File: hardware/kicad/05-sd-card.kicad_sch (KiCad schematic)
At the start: 1 part, among them U6 SD_Card_SPI

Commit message: fix(schematic): sync GPIO labels with config.py (SD_MOSI/MISO, BTN_L/R)
Schematic sheets had stale GPIO annotations:
- SD_MOSI: GPIO36 → GPIO44
- SD_MISO: GPIO37 → GPIO43
- BTN_L: GPIO35 → GPIO45
- BTN_R: GPIO43 → GPIO3

Also update /doc skill to regenerate schematics before auditing.

Co-Authored-By: Claude Opus 4.6 (1M context) <noreply@anthropic.com>
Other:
- note added: "GPIO43"
- note added: "GPIO44"
- note removed: "GPIO36"
- note removed: "GPIO37"
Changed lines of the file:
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@@
   (wire (pts (xy 158.16 106.19) (xy 183.16 106.19)) (stroke (width 0) (type default)))
   (global_label "SD_MOSI" (shape bidirectional) (at 183.16 106.19 0) (effects (font (size 1.27 1.27))) (property "Intersheetrefs" "" (at 0 0 0) (effects (font (size 1.27 1.27)) hide)))
-  (text "GPIO36" (at 198.16 106.19 0) (effects (font (size 1.5 1.5)) (justify left)))
+  (text "GPIO44" (at 198.16 106.19 0) (effects (font (size 1.5 1.5)) (justify left)))
   (wire (pts (xy 158.16 110) (xy 183.16 110)) (stroke (width 0) (type default)))
   (global_label "SD_MISO" (shape bidirectional) (at 183.16 110 0) (effects (font (size 1.27 1.27))) (property "Intersheetrefs" "" (at 0 0 0) (effects (font (size 1.27 1.27)) hide)))
-  (text "GPIO37" (at 198.16 110 0) (effects (font (size 1.5 1.5)) (justify left)))
+  (text "GPIO43" (at 198.16 110 0) (effects (font (size 1.5 1.5)) (justify left)))
   (wire (pts (xy 158.16 113.81) (xy 183.16 113.81)) (stroke (width 0) (type default)))
   (global_label "SD_CLK" (shape bidirectional) (at 183.16 113.81 0) (effects (font (size 1.27 1.27))) (property "Intersheetrefs" "" (at 0 0 0) (effects (font (size 1.27 1.27)) hide)))

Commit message: fix(hw): R4 audit — schematic↔PCB sync guard + 4 fixes + R4-CRIT-1 false-positive closure
Round 4 of the hardware audit found four real schematic/PCB drift bugs
that rounds 1-3 missed because no check cross-validated the two Python
generators. A fifth finding (R4-CRIT-1, "FPC pinout mismatch") turned
out to be a FALSE POSITIVE caused by the landscape FPC pin reversal
(connector_pad = 41 − panel_pin) — verified programmatically against
all 40 J4 pads of the panel datasheet in components.md.

Fixes applied:
  R4-HIGH-1  USBLC6 (U4) + R22/R23 instantiated in power_supply.py —
             previously only in routing.py, invisible to schematic
             review.
  R4-HIGH-2  Display module symbol ref renamed U4 → DS1 in display.py.
             U4 is now cleanly owned by the physical USBLC6 TVS.
  R4-HIGH-3  PAM8403 R20/R21 input bias moved from GND to VREF
             (pin 8) per the datasheet single-ended app circuit.
  R4-CRIT-1  CLOSED as false positive. Both display.py (panel-side)
             and datasheet_specs.py (connector-side) were correct all
             along. Added 41-N reversal documentation at the top of
             both files so the mistake can't be re-raised.
  ERC CRIT   Pre-existing "Power output ↔ Power output" on +5V was
             PWR_FLAG duplicating IP5306 VOUT (already power_out in the
             library symbol). Removed the PWR_FLAG. ERC now 0 critical.

Incidental cleanups required by the new sync guard:
  - mcu.py R3 (external EN pull-up) removed from schematic — already
    DNP in BOM because the WROOM-1 module has an internal pull-up.
  - controls.py D1 BAT54C (MENU combo diode) instantiated in schematic
    to match the PCB routing. MENU button wiring simplified to the
    MENU_K node; there is no dedicated BTN_MENU GPIO (firmware detects
    START+SELECT combo).
  - power_supply.py USB_CC1 / USB_CC2 global labels added so the
    connector-net coverage check sees the full USB-C net set.
  - display.py docstring expanded with the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
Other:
- note added: "v2 TODO: add local 100nF bypass near U6 VCC (R4-MED-1)"
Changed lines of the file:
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@@
   (wire (pts (xy 118 113.81) (xy 137.84 113.81)) (stroke (width 0) (type default)))
   (text "GPIO39" (at 90 115 0) (effects (font (size 1.5 1.5)) (justify left)))
+  (text "v2 TODO: add local 100nF bypass near U6 VCC (R4-MED-1)" (at 90 120 0) (effects (font (size 1.5 1.5)) (justify left)))
   (text "Design Notes:" (at 30 160 0) (effects (font (size 2.54 2.54) bold) (justify left)))
   (text "- SPI bus @ up to 40MHz (ESP32-S3 max for SD)" (at 30 168 0) (effects (font (size 2.54 2.54)) (justify left)))

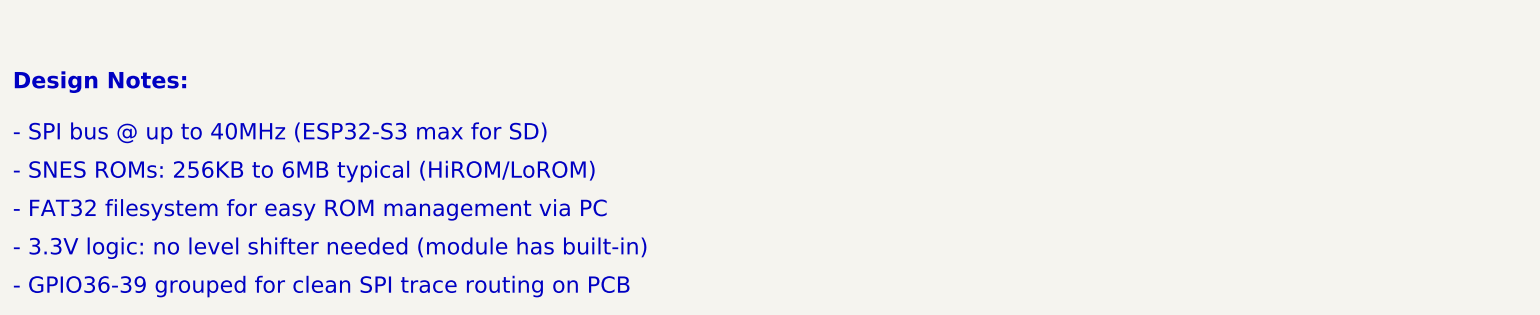
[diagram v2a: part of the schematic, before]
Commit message: docs(R10): close 8 LOW-severity doc-drift findings from Layer 2 audit
Round 10 hardware-audit Layer 2 prose pass found no functional bugs
(0 CRIT/HIGH/MED) but surfaced 8 stale comments and doc-drift items
across schematic generator text labels, datasheet_specs.py function
strings, verify_strapping_pins.py RC timing math, and
snes-optimization.md. All fixed in this single commit — no PCB
regeneration, no routing/geometry changes.

- R10-LOW-1: mcu.py GPIO table labeled "GPIO26-32 = Octal PSRAM" but
  those are actually Octal Flash pins on ESP32-S3-WROOM-1 N16R8.
  PSRAM is on GPIO33-37. Relabeled to show both Flash and PSRAM.

- R10-LOW-2: audio.py I2S bus reference text said "BCLK 1.411MHz @
  44.1kHz" but firmware uses PDM TX (no BCLK/LRCK) at 32kHz.
  Relabeled GPIO15/16 as UNUSED with a v2-reuse note (candidates for
  ADC2 battery voltage). Dead-net removal deferred to v2 respin.

- R10-LOW-3: sd_card.py said "SPI @ up to 40MHz" but firmware runs
  20MHz (R2-MED-5 trace-length cap). Updated design-note text.

- R10-LOW-4: sd_card.py said "GPIO36-39 grouped for clean SPI" but
  actual SPI pins are GPIO38/39 (CLK/CS) + GPIO43/44 (MISO/MOSI) —
  split across the WROOM-1 module. Updated design-note text.

- R10-LOW-5: datasheet_specs.py J4 pads 15/16 function strings said
  "NC (IM0/IM1 mode select)" but after the 41-N panel pin reversal
  those pads correspond to DB9/DB8 (unused upper data bits in 8-bit
  8080 mode). IM0/IM1 are actually on J4 pads 3/2. Fixed function
  strings with a comment explaining the 41-N mapping.

- R10-LOW-6: datasheet_specs.py U5 block comment said "left channel
  only: OUTL+ → SPK+, OUTL- → SPK-" but the pad map wires SPK± to
  OUTR+/OUTR- (pins 14/16). OUTL+/- are floating. Rewrote the
  comment + pin 1/3 function strings to match the actual wiring.

- R10-LOW-7: verify_strapping_pins.py test_en_rc_delay() computed
  tau = 10kΩ·100nF = 1ms assuming external R3, but R4 closed R3 as
  DNP and the WROOM-1 module integrates a ~45kΩ EN pull-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
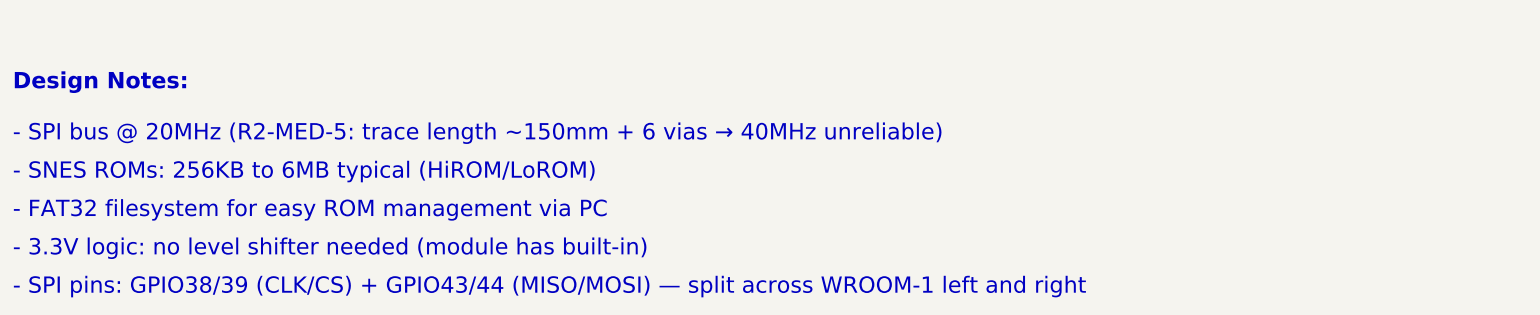
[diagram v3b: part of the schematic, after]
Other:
- note added: "- SPI bus @ 20MHz (R2-MED-5: trace length ~150mm + 6 vias → 40MHz unreliable)"
- note added: "- SPI pins: GPIO38/39 (CLK/CS) + GPIO43/44 (MISO/MOSI) — split across WROOM-1 left and right"
- note removed: "- GPIO36-39 grouped for clean SPI trace routing on PCB"
- note removed: "- SPI bus @ up to 40MHz (ESP32-S3 max for SD)"
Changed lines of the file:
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@@
   (text "v2 TODO: add local 100nF bypass near U6 VCC (R4-MED-1)" (at 90 120 0) (effects (font (size 1.5 1.5)) (justify left)))
   (text "Design Notes:" (at 30 160 0) (effects (font (size 2.54 2.54) bold) (justify left)))
-  (text "- SPI bus @ up to 40MHz (ESP32-S3 max for SD)" (at 30 168 0) (effects (font (size 2.54 2.54)) (justify left)))
+  (text "- SPI bus @ 20MHz (R2-MED-5: trace length ~150mm + 6 vias → 40MHz unreliable)" (at 30 168 0) (effects (font (size 2.54 2.54)) (justify left)))
   (text "- SNES ROMs: 256KB to 6MB typical (HiROM/LoROM)" (at 30 174 0) (effects (font (size 2.54 2.54)) (justify left)))
   (text "- FAT32 filesystem for easy ROM management via PC" (at 30 180 0) (effects (font (size 2.54 2.54)) (justify left)))
   (text "- 3.3V logic: no level shifter needed (module has built-in)" (at 30 186 0) (effects (font (size 2.54 2.54)) (justify left)))
-  (text "- GPIO36-39 grouped for clean SPI trace routing on PCB" (at 30 192 0) (effects (font (size 2.54 2.54)) (justify left)))
+  (text "- SPI pins: GPIO38/39 (CLK/CS) + GPIO43/44 (MISO/MOSI) — split across WROOM-1 left and right" (at 30 192 0) (effects (font (size 2.54 2.54)) (justify left)))
   (sheet_instances (path "/" (page "5")))
 )

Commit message: sch(layout): fix annotation overlaps across all 6 sheets — reflow to A3 where needed
Root cause: multiple sheets had annotation text boxes placed too close
to each other or to component symbols/net labels. On the live website
this rendered as strings running through each other and through
component pins — unreadable in the schematic viewer.

Per-sheet fixes:

* Sheet 1 — Power Supply
  - Upgraded to A3 landscape (was A4). USB ESD (U4/R22/R23) had
    been placed at (45, 160) directly on top of SW_PWR, C1, U3
    and C2 — all at y=160. There was no room on A4 to fit both
    the input stage (USB-C + IP5306 + battery) and the output
    stage (AMS1117 + LEDs + power switch + USB ESD) with clean
    annotations.
  - USB ESD block relocated to its own dedicated row (y=140).
  - CHARGING INDICATOR LEDs moved to a dedicated right-side zone
    (x=275, y=145) so they no longer collide with USB ESD.
  - POWER SWITCH moved to its own right-side zone (x=285, y=200)
    so its long "v1 as-built" help text no longer crosses through
    C1 / U3 (AMS1117) / C2.
  - VOLTAGE REGULATOR title + AMS1117 area pushed down (y=175 /
    y=200) with DESIGN NOTES following (y=240).
  - C18 (BAT bypass) moved left of Q1, out of the "P-MOSFET RPP /
    SI2301CDS" label zone; C27 (HF bypass) spaced further from C19
    (was 15mm gap, now 22mm) so "VOUT bulk" label no longer runs
    into "HF bypass".
  - Q1 dual annotation stacked with 3mm vertical spacing (was 2mm).
  - R24 label moved BELOW its symbol as "Q1 gate PD".
  - J3 / BT1 pushed further right (jst_x=268, bt_x=315) to use A3
    width and clear the Q1 cluster.

* Sheet 2 — MCU (ESP32-S3)
  - EN pull-up annotation shortened + moved up so it no longer
    collides with the "RC reset delay" label below.
  - BOOT switch pushed further down (c_en_y + 55) and left of the
    RESET switch so its BTN_SELECT glabel and help text no longer
    overlap the DISPLAY / AUDIO / CONTROLS annotation column. Help
    text now sits below the switch in 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
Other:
- note added: "- v2 TODO (R4-MED-1): add local 100nF bypass within 5 mm of U6 VCC"
- note removed: "v2 TODO: add local 100nF bypass near U6 VCC (R4-MED-1)"
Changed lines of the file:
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@@
   (wire (pts (xy 118 113.81) (xy 137.84 113.81)) (stroke (width 0) (type default)))
   (text "GPIO39" (at 90 115 0) (effects (font (size 1.5 1.5)) (justify left)))
-  (text "v2 TODO: add local 100nF bypass near U6 VCC (R4-MED-1)" (at 90 120 0) (effects (font (size 1.5 1.5)) (justify left)))
   (text "Design Notes:" (at 30 160 0) (effects (font (size 2.54 2.54) bold) (justify left)))
   (text "- SPI bus @ 20MHz (R2-MED-5: trace length ~150mm + 6 vias → 40MHz unreliable)" (at 30 168 0) (effects (font (size 2.54 2.54)) (justify left)))
@@
   (text "- 3.3V logic: no level shifter needed (module has built-in)" (at 30 186 0) (effects (font (size 2.54 2.54)) (justify left)))
   (text "- SPI pins: GPIO38/39 (CLK/CS) + GPIO43/44 (MISO/MOSI) — split across WROOM-1 left and right" (at 30 192 0) (effects (font (size 2.54 2.54)) (justify left)))
+  (text "- v2 TODO (R4-MED-1): add local 100nF bypass within 5 mm of U6 VCC" (at 30 198 0) (effects (font (size 2.54 2.54)) (justify left)))
   (sheet_instances (path "/" (page "5")))
 )

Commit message: sch+tools: fix schematic/PCB pin divergence, recalibrate USB check to Full Speed, make verify-all mean "all"
Failure 1 — verify_netlist_diff T4 (4 mismatches + 2 suppression mechanisms)

Schematic side was wrong in every case; decided from datasheets, not convenience.

* U4 (USBLC6-2SC6, ST doc ID 11265 Rev 5): pins 1/6 are one internal
  I/O node and pins 3/4 the other. The schematic had USB_DM_MCU on
  pin 6 and USB_DP_MCU on pin 4, which shorts R23/R22 out inside the
  package. Both pins of each pair now sit on the connector-side net,
  matching routing.py and hardware/datasheet_specs.py.
* U4 pin 5 is the VBUS clamp reference; the schematic tied it to +5V,
  the IP5306 boost OUTPUT, which is live with no cable attached. Now
  VBUS, as the board already had it.
* U3 (AMS1117): the library symbol used the generic 1=VIN/2=GND/3=VOUT
  numbering. The SOT-223 datasheet land is 1=GND/2=VOUT/3=VIN plus a
  tab (4) that is VOUT. Symbol renumbered, tab pin added; drawing
  unchanged.
* C24/C27/C21 and the twelve button pull-ups R4..R15 had pin 1 and
  pin 2 the opposite way round from their footprints. Symbol
  placement now supports a rotation angle, and these symmetric
  two-terminal parts are placed at 180 deg so the pin numbers agree
  with the pads without altering how the sheet looks.

Real schematic defects found while doing the above:

* Sheets 4 and 5 dropped a GND stub straight through the anchor of the
  label below it: SD_CS was shorted to GND on the SD sheet and the
  PAM8403 audio input was shorted to GND on the audio sheet.
* R22 and R23 were wired with horizontal stubs against a symbol whose
  pins are vertical, so both series termination resistors were
  completely floating in the exported netlist.
* Same class: C22 (the audio DC-block) and the top terminals of
  R20/R21 were attached to nothing.
* The display sheet walked the FPC symbol pins backwards and ran one
  step off the end, so LCD_D7 never reached J4 — the schematic showed
  a 7-bit data bus. I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
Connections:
- net SD_CS: no longer U6.2 (GND)
- new net GND: U6.2 (GND)
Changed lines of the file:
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@@
   (global_label "+3V3" (shape input) (at 118 106.19 0) (effects (font (size 1.27 1.27))) (property "Intersheetrefs" "" (at 0 0 0) (effects (font (size 1.27 1.27)) hide)))
   (wire (pts (xy 118 106.19) (xy 137.84 106.19)) (stroke (width 0) (type default)))
-  (symbol (lib_id "GND") (at 118 118 0) (unit 1) (exclude_from_sim no) (in_bom no) (on_board no) (dnp no) (property "Reference" "#PWR001" (at 118 116 0) (effects (font (size 1.27 1.27)) hide)) (property "Value" "GND" (at 118 120 0) (effects (font (size 1.27 1.27)) hide)) (pin "1"))
-  (wire (pts (xy 137.84 110) (xy 118 110)) (stroke (width 0) (type default)))
-  (wire (pts (xy 118 110) (xy 118 118)) (stroke (width 0) (type default)))
+  (global_label "GND" (shape input) (at 118 110 0) (effects (font (size 1.27 1.27))) (property "Intersheetrefs" "" (at 0 0 0) (effects (font (size 1.27 1.27)) hide)))
+  (wire (pts (xy 118 110) (xy 137.84 110)) (stroke (width 0) (type default)))
   (text "SPI bus:" (at 166 100 0) (effects (font (size 2 2) bold) (justify left)))
   (wire (pts (xy 158.16 106.19) (xy 183.16 106.19)) (stroke (width 0) (type default)))
